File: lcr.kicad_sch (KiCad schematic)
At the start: 45 parts, among them J5 Conn_01x04_Pin, J6 Conn_01x06_Pin, J7 USB_C_Receptacle_USB2.0_14P, SW2 SW_Push, SW3 SW_Push, U10 USBLC6-2SC6, U13 UMW HT7836-A, U5 TLV75733PDBV, U8 STM32G431CBT6, Y3 8 MHz

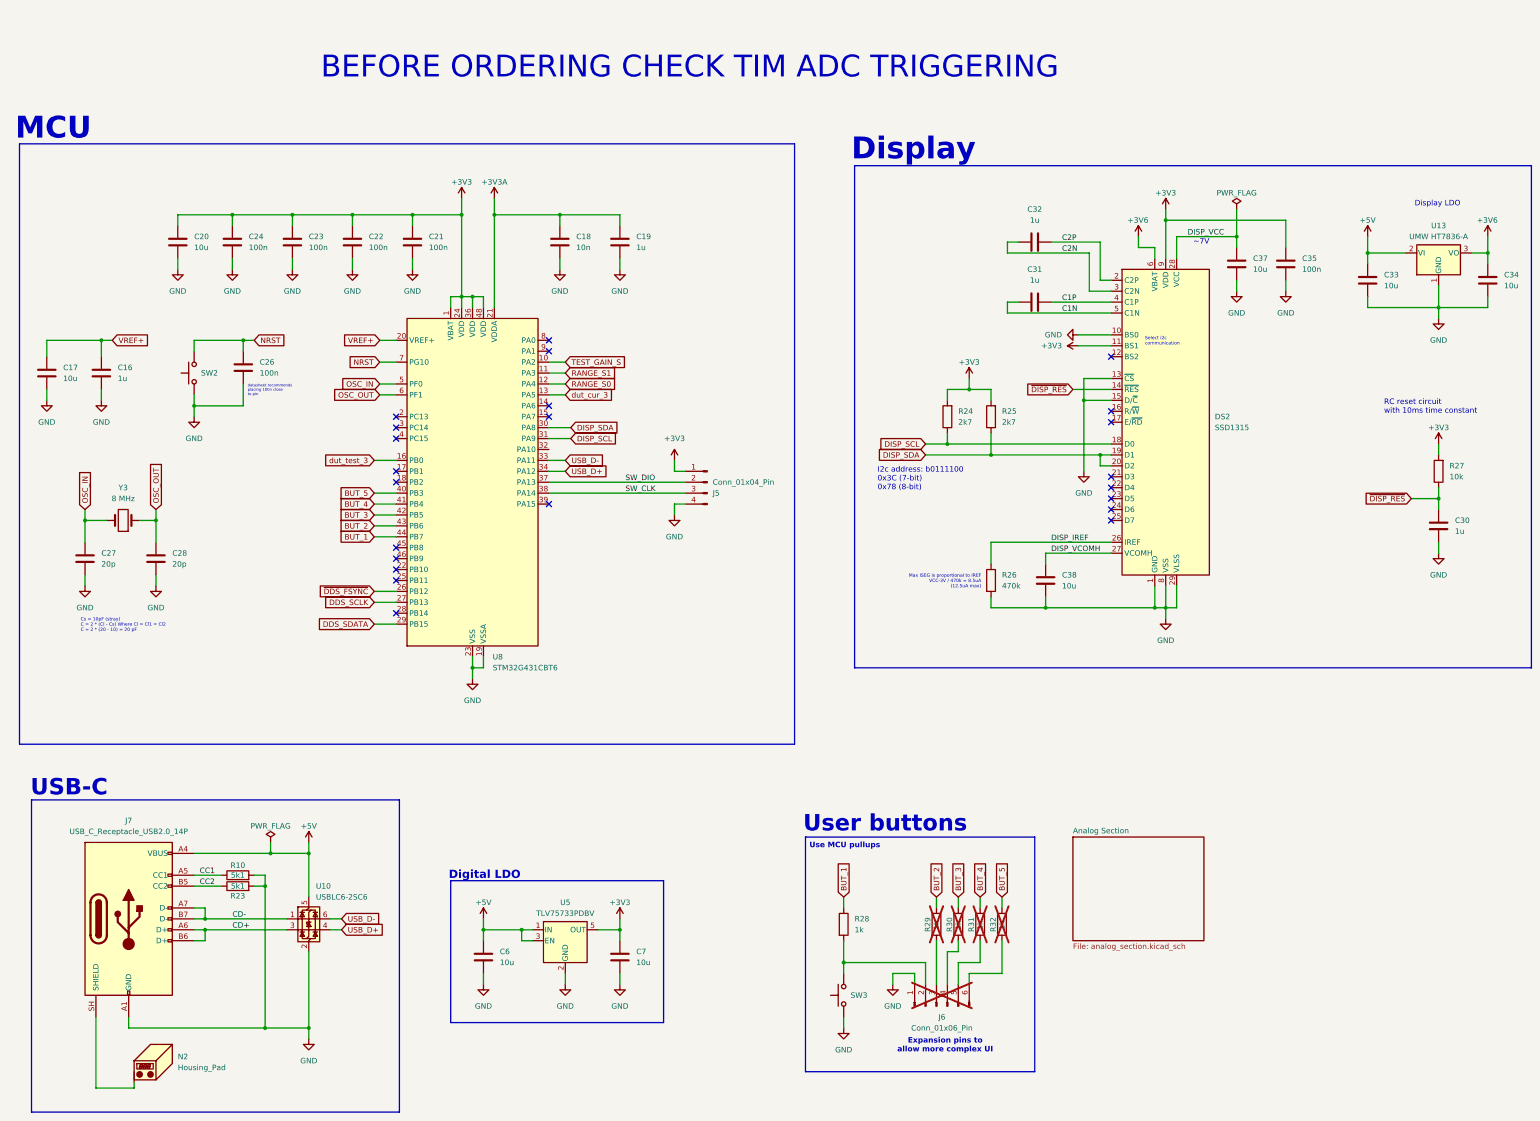
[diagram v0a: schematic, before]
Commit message: Did some routing
Commiting before changing display from i2c to spi
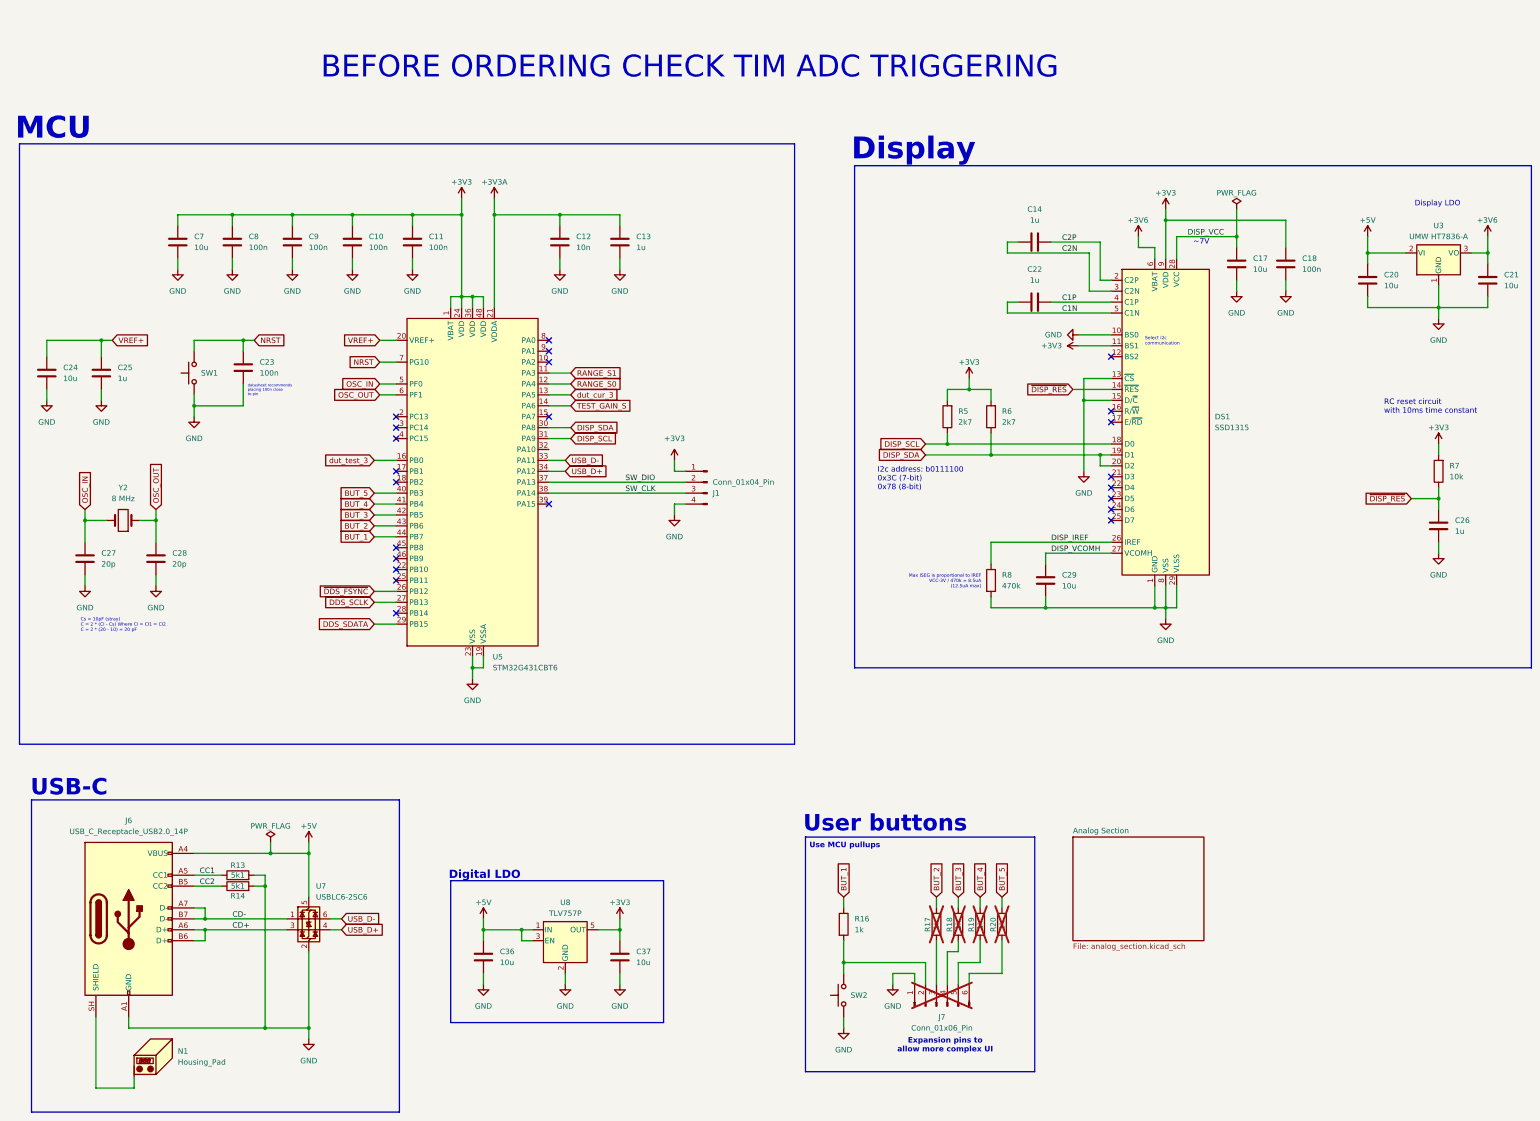
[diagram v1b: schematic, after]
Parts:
- removed U5: TLV75733PDBV, Package_TO_SOT_SMD:SOT-23-5, symbol Regulator_Linear:TLV75733PDBV
- added U8: TLV757P, Package_TO_SOT_SMD:SOT-23-5, symbol CustomSymbols:TLV757P
- U3: renamed from U13; Already Have (none) -> 0; LCSC PART # (none) -> C347196
- renumbered C22 to C10, C21 to C11, C18 to C12, C19 to C13, C32 to C14, C37 to C17, C35 to C18, C33 to C20, C34 to C21, C31 to C22, C26 to C23, C17 to C24, C16 to C25, C30 to C26, C38 to C29, C6 to C36, C7 to C37, C20 to C7, C24 to C8, C23 to C9, DS2 to DS1, J5 to J1, J7 to J6, J6 to J7, N2 to N1, R10 to R13, R23 to R14, R28 to R16, R29 to R17, R30 to R18, R31 to R19, R32 to R20, R24 to R5, R25 to R6, R27 to R7, R26 to R8, SW2 to SW1, SW3 to SW2, U8 to U5, U10 to U7, Y3 to Y2
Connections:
- net +3V3: now also U8.5 (OUT)
- net +5V: now also U8.1 (IN), U8.3 (EN)
- net GND: now also U8.2 (GND), U8.4 (NC)
- net TEST_GAIN_S: now also U5.14 (PA6); no longer U5.10 (PA2)
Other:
- moved on the sheet: N1

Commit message: Done
Schematics and PCB are "done".
Meaning I've just finished but need to review
the design before it's ready to order.
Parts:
- removed J7: Conn_01x06_Pin, Connector_PinHeader_2.54mm:PinHeader_1x06_P2.54mm_Vertical, symbol Connector:Conn_01x06_Pin
- removed R17, R18, R19, R20: 1k, Resistor_SMD:R_0603_1608Metric, symbol Device:R
- removed R5, R6: 2k7, Resistor_SMD:R_0603_1608Metric, symbol Device:R
- added H1, H2, H3, H4: MountingHole, MountingHole:MountingHole_3.2mm_M3, symbol Mechanical:MountingHole
- added TP13, TP14: GND, TestPoint:TestPoint_Pad_D1.5mm, symbol Connector:TestPoint
- added TP2: MCO, TestPoint:TestPoint_Pad_D1.5mm, symbol Connector:TestPoint
- added TP3: PB6, TestPoint:TestPoint_Pad_D1.5mm, symbol Connector:TestPoint
- renumbered R13 to R11, R14 to R12, R16 to R14, R7 to R5, R8 to R6
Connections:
- net BUT_2 is gone; now on net BUT_1: U5.43 (PB6)
- net +3V3: now also DS1.10 (BS0); no longer DS1.11 (BS1)
- net BUT_1: no longer U5.44 (PB7)
- net GND: now also DS1.11 (BS1), TP13.1, TP14.1; no longer DS1.10 (BS0), DS1.13 (~{CS})
- net TEST_GAIN_S: now also U5.25 (PB11); no longer U5.14 (PA6)
- net ~{DISP_CS}: now reaches U5.39 (PA15)
- net ~{DISP_CS}: now also DS1.13 (~{CS})
- net BUT_3 renamed DISP_DAT
- net DISP_DAT: now also DS1.19 (D1)
- net BUT_4: no longer names the net of U5.41 (PB4)
- net BUT_5 renamed DISP_SCK
- net DISP_SCK: now also DS1.18 (D0)
- net DISP_SCL: no longer names the net of U5.31 (PA9)
- net DISP_SCL: no longer DS1.18 (D0)
- removed net DISP_SDA: DS1.19 (D1), DS1.20 (D2), U5.30 (PA8)
- new net MCO: TP2.1, U5.30 (PA8)
- new net PB6: TP3.1, U5.44 (PB7)
- no-connect marks 23 -> 25
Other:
- note added: "Max ISEG is proportional to IREF IREF = VCC-3V / 470k = 8.5uA (12.5uA max)"
- note added: "Mounting"
- note added: "Select 3 wire SPI communication"
- note added: "User button use MCU pullup"
- note removed: "Expansion pins to allow more complex UI"
- note removed: "I2c address: b0111100 0x3C (7-bit) 0x78 (8-bit)"
- note removed: "Max ISEG is proportional to IREF VCC-3V / 470k = 8.5uA (12.5uA max)"
- note removed: "Select i2c communication"
- note removed: "Use MCU pullups"
- note removed: "User buttons"
- note removed: "datasheet recommends placing 100n close to pin"
- title: LCR Digital Section -> LCR Main Section (digital)
- moved on the sheet: C14, C17, C18, C20, C21, C22, C26, C29, C36, C37, DS1, R14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

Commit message: Added polish
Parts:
- removed C17, C29: 10u, Capacitor_SMD:C_0603_1608Metric, symbol Device:C
- added C46, C47: 4u7, Capacitor_SMD:C_0603_1608Metric, symbol Device:C
- added D6: LED, LED_SMD:LED_0603_1608Metric, symbol Device:LED
- added R29: 1k, Resistor_SMD:R_0603_1608Metric, symbol Device:R
- renumbered C9 to C10, C10 to C11, C11 to C12, C12 to C13, C13 to C14, C18 to C16, C20 to C19, C21 to C20, C14 to C7, C7 to C8, C8 to C9, R14 to R15, R11 to R17, R12 to R19, R5 to R6, R6 to R8, TP13 to TP7, TP14 to TP8, U8 to U7, U7 to U8
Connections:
- net +3V3: now also D6.2 (A)
- net DISP_VCC: now also C47.1
- net DISP_VCOMH: now also C46.1
- net GND: now also C46.2, C47.2, R29.2
- new net: D6.1 (K), R29.1
- no-connect marks 25 -> 26
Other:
- note added: "BEFORE ORDERING CHECK TIM ADC TRIGGERING POWER SUPPLY RIPPLE RESISTOR SWITCHES"
- note removed: "BEFORE ORDERING CHECK TIM ADC TRIGGERING"
- moved on the sheet: TP7, TP8

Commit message: Changed range resistor selector design
Changed range resistor selector from an analog mux
to a MOSFET BPS design. This should improve on resistance, linearity,
and temperature stability for the range resistors.
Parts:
- D6: Already Have (none) -> 1
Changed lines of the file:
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@@
 	(title_block
 		(title "LCR Main Section (digital)")
-		(date "2026-04-12")
+		(date "2026-04-26")
 		(company "LWQ")
 	)
@@
 			(at 151.13 254 0)
 			(hide yes)
+			(show_name no)
+			(do_not_autoplace no)
+			(effects
+				(font
+					(size 1.27 1.27)
+				)
+			)
+		)
+		(property "Already Have" "1"
+			(at 151.13 254 0)
+			(hide yes)

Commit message: Started new layout
Range resistors now use MOSFET BPS.
Currently there's no protection for over voltage on the opamp or mcu
inputs, so that needs to be done.
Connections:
- net TEST_GAIN_S: now also U5.10 (PA2); no longer U5.25 (PB11)
- net dut_test_3 renamed dut_test_4
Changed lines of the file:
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@@
-	)
-	(no_connect
-		(at 156.21 97.79)
 	)
 	(no_connect
@@
 	)
 	(no_connect
+		(at 120.65 148.59)
+	)
+	(no_connect
 		(at 156.21 110.49)
 	)
@@
 	(wire
 		(pts
-			(xy 115.57 148.59) (xy 120.65 148.59)
-		)
-		(stroke
-			(width 0)
-			(type default)
-		)
-	)
-	(wire
-		(pts
 			(xy 144.78 254) (xy 144.78 251.46)
 		)
@@
 		(pts
 			(xy 138.43 168.91) (xy 138.43 171.45)
+		)
+		(stroke
+			(width 0)
+			(type default)
+		)
+	)
+	(wire
+		(pts
+			(xy 156.21 97.79) (xy 161.29 97.79)
 		)
 		(stroke
@@
 		)
 	)
-	(global_label "TEST_GAIN_S"
-		(shape input)
-		(at 115.57 148.59 180)
-		(fields_autoplaced yes)
-		(effects
-			(font
-				(size 1.27 1.27)
-			)
-			(justify right)
-		)
-		(property "Intersheetrefs" "${INTERSHEET_REFS}"
-			(at 100.8525 148.59 0)
-			(hide yes)
-			(show_name no)
-			(do_not_autoplace no)
-			(effects
-				(font
-					(size 1.27 1.27)
-				)
-				(justify right)
-			)
-		)
-	)
 	(global_label "OSC_IN"
 		(shape input)
@@
 		)
 	)
-	(global_label "dut_test_3"
+	(global_label "dut_test_4"
 		(shape input)
 		(at 115.57 120.65 180)
@@
 			(hide yes)
 			(show_name no)
+			(do_not_autoplace no)
+			(effects
+				(font
+					(size 1.27 1.27)
+				)
+				(justify left)
+			)
+		)
+	)
+	(global_label "TEST_GAIN_S"
+		(shape input)
+		(at 161.29 97.79 0)
+		(fields_autoplaced yes)
+		(effects
+			(font
+				(size 1.27 1.27)
+			)
+			(justify left)
+		)
+		(property "Intersheetrefs" "${INTERSHEET_REFS}"
+			(at 176.0075 97.79 0)
+			(hide yes)
+			(show_name no)

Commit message: Added protection to MCU analog inputs
DUT and test voltages now use clamping diodes to protect the MCU from
voltages less than 0V and greater than 3.3V.
Started laying out again, but thinking of trying something different
with the layou of the range resistors around the 1st opamp.
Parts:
- renumbered C11 to C10, C12 to C11, C13 to C12, C14 to C13, C47 to C15, C19 to C17, C20 to C18, C22 to C21, C23 to C25, C24 to C26, C25 to C27, C26 to C28, C27 to C29, C28 to C30, C46 to C31, C36 to C41, C37 to C42, C7 to C6, C8 to C7, C9 to C8, C10 to C9, D6 to D10, R15 to R10, R17 to R14, R19 to R16, R29 to R19, R6 to R5, TP8 to TP10, TP7 to TP9, U3 to U2, U7 to U8, U8 to U9
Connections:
- net dut_cur_3 renamed dut_cur_4

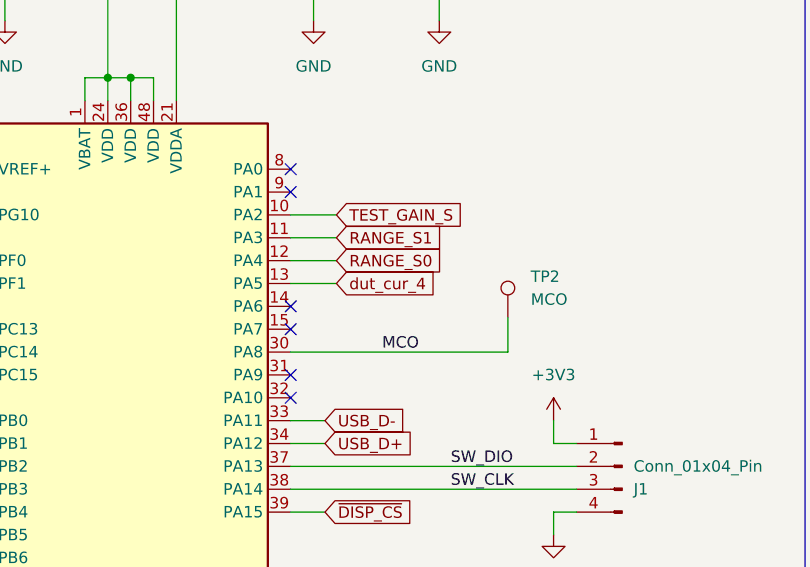
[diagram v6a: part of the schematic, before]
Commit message: Done new layout
Now need to polish again. Also should test BPS
in the flesh and innevetably scrap half the current schematic
and layout when it doesn't work as expected.
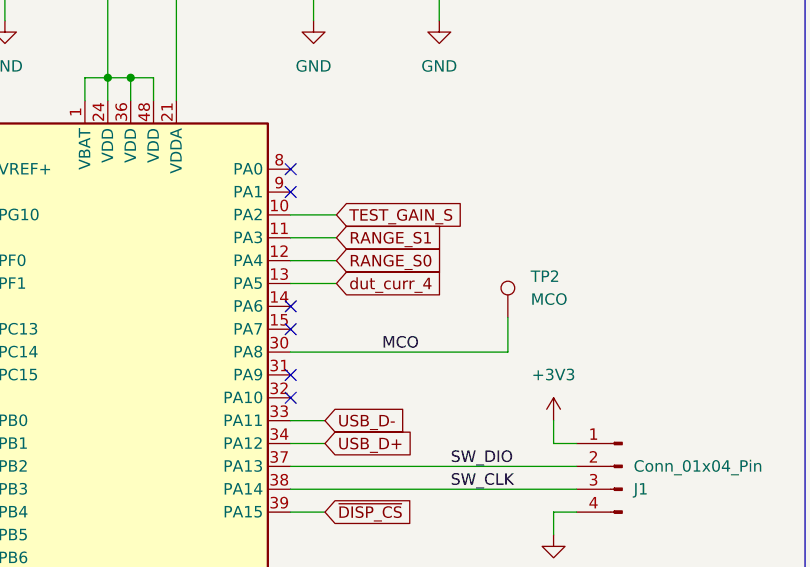
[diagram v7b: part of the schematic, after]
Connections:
- net dut_cur_4 renamed dut_curr_4
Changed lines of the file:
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@@
 		)
 	)
-	(global_label "dut_cur_4"
+	(global_label "dut_curr_4"
 		(shape input)
 		(at 161.29 105.41 0)
@@
 		)
 		(property "Intersheetrefs" "${INTERSHEET_REFS}"
-			(at 173.4674 105.41 0)
+			(at 174.2536 105.41 0)
 			(hide yes)
 			(show_name no)
